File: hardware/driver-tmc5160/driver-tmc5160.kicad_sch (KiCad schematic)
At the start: 54 parts, among them M1 Micro-Fit 3.0, T1 GND, T10 STEP, T11 GND, T12 DIR, T13 EN, T14 SPI_MODE, T15 SD_MODE, T16 DIAG0, T17 DIAG1, T18 ENCA, T19 ENCB, T2 CLK, T20 ENCN, T3 12V, T4 SCK, T5 GND, T6 SDI, T7 SDO, T8 VCC, T9 CS0, U1 TMC5160A-TA

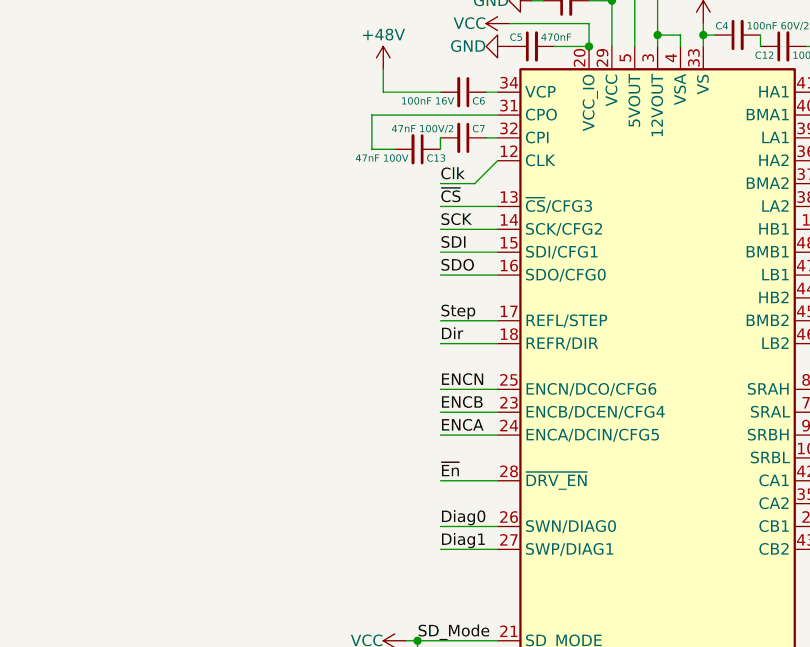
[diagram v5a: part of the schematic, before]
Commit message: added more 3D models and created first few renders
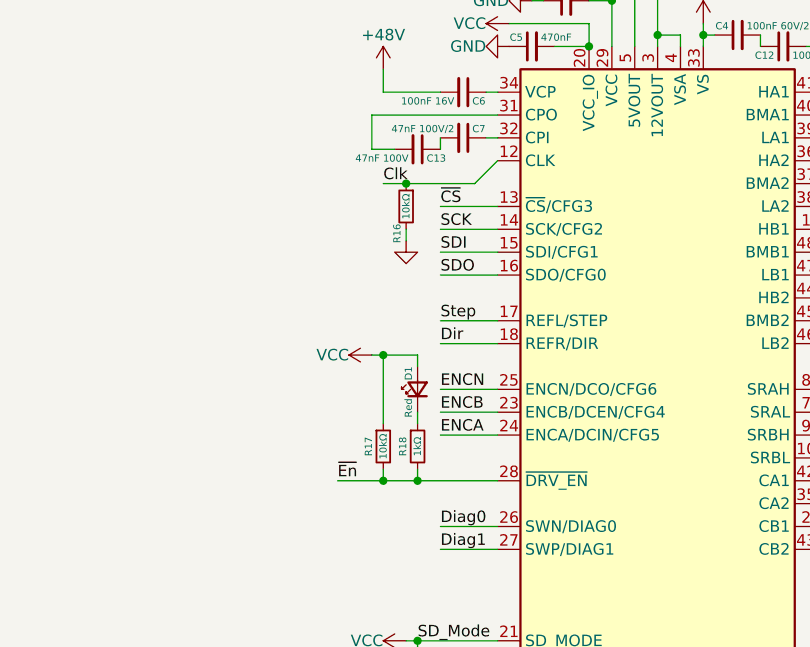
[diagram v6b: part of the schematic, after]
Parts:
- added D1: Red, AlphaLib:0603LED, symbol Device:LED_Small
- added R16, R17: 10kΩ, AlphaLib:0402R, symbol Device:R_Small
- added R18: 1kΩ, AlphaLib:0402R, symbol Device:R_Small
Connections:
- net Clk: now also R16.1
- net GND: now also R16.2
- net VCC: now also D1.2 (A), R17.1
- net ~{En}: now also R17.2, R18.2
- new net: D1.1 (K), R18.1

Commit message: adopt corevus-g designation for current mainboard, cleanup
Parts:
- C3, C5: value 470nF -> 1µF
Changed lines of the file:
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@@
       (effects (font (size 0.8 0.8)) (justify left))
     )
-    (property "Value" "470nF" (at 135.62 98.06 90)
+    (property "Value" "1µF" (at 135.62 98.06 90)
       (effects (font (size 0.8 0.8)) (justify right))
     )
@@
       (effects (font (size 0.8 0.8)) (justify left))
     )
-    (property "Value" "470nF" (at 131.81 103.14 90)
+    (property "Value" "1µF" (at 131.81 103.14 90)
       (effects (font (size 0.8 0.8)) (justify right))
     )
@@
   (symbol (lib_id "Driver_Motor:TMC5160A-TA") (at 144.78 142.24 0) (unit 1)
     (in_bom yes) (on_board yes) (dnp no) (fields_autoplaced)
-    (property "Reference" "U1" (at 149.3394 180.34 0)
+    (property "Reference" "U1" (at 149.5141 180.34 0)
       (effects (font (size 1.27 1.27)) (justify left))
     )
-    (property "Value" "TMC5160A-TA" (at 149.3394 182.88 0)
+    (property "Value" "TMC5160A-TA" (at 149.5141 182.88 0)
       (effects (font (size 1.27 1.27)) (justify left))
     )
